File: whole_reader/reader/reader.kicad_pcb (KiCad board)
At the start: 2 copper layers, 50 x 58.5 mm, 66 parts, among them U1 LM386M-1, U2 STM32F103C8T6, U3 MCP16301Hx-xCH, U4 MAX3232, Y1 16MHz

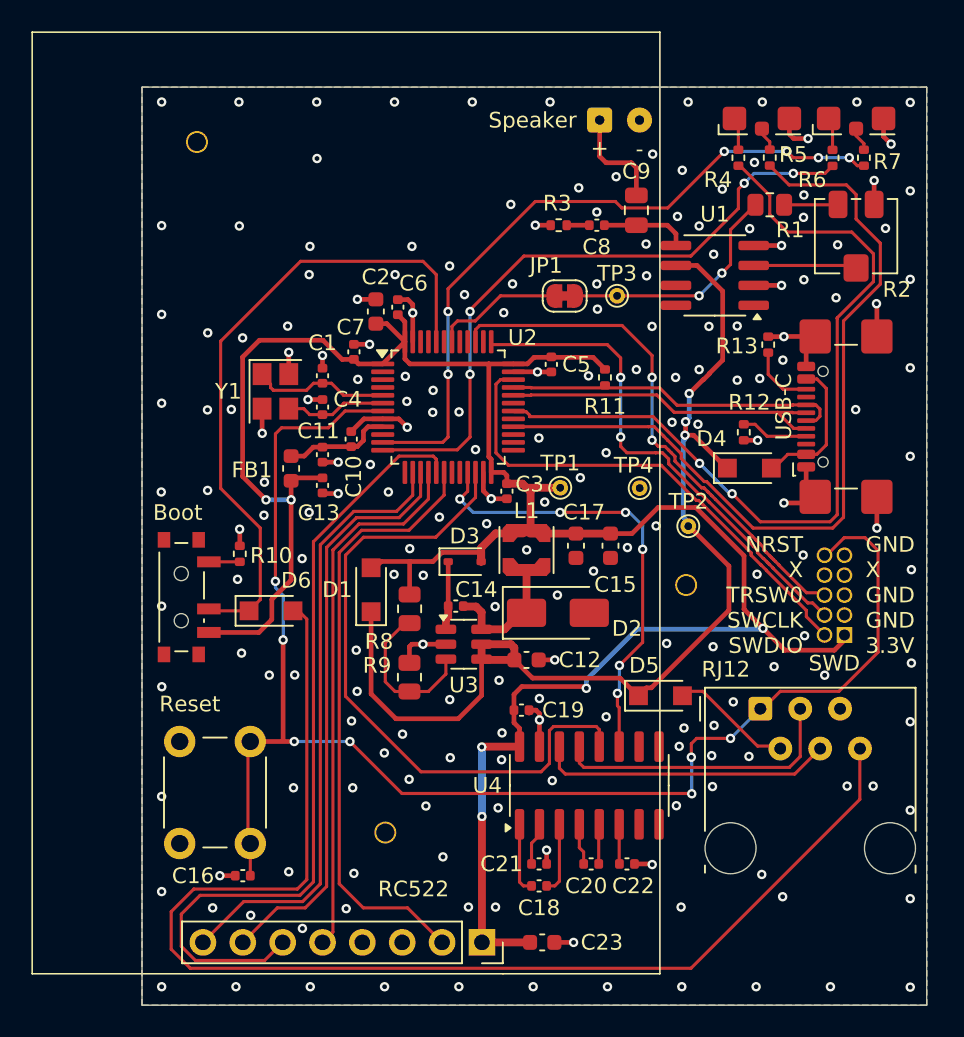
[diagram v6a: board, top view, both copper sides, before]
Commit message: Úprava rozloženia dosky a pridanie TP5 pre RFID_IRQ
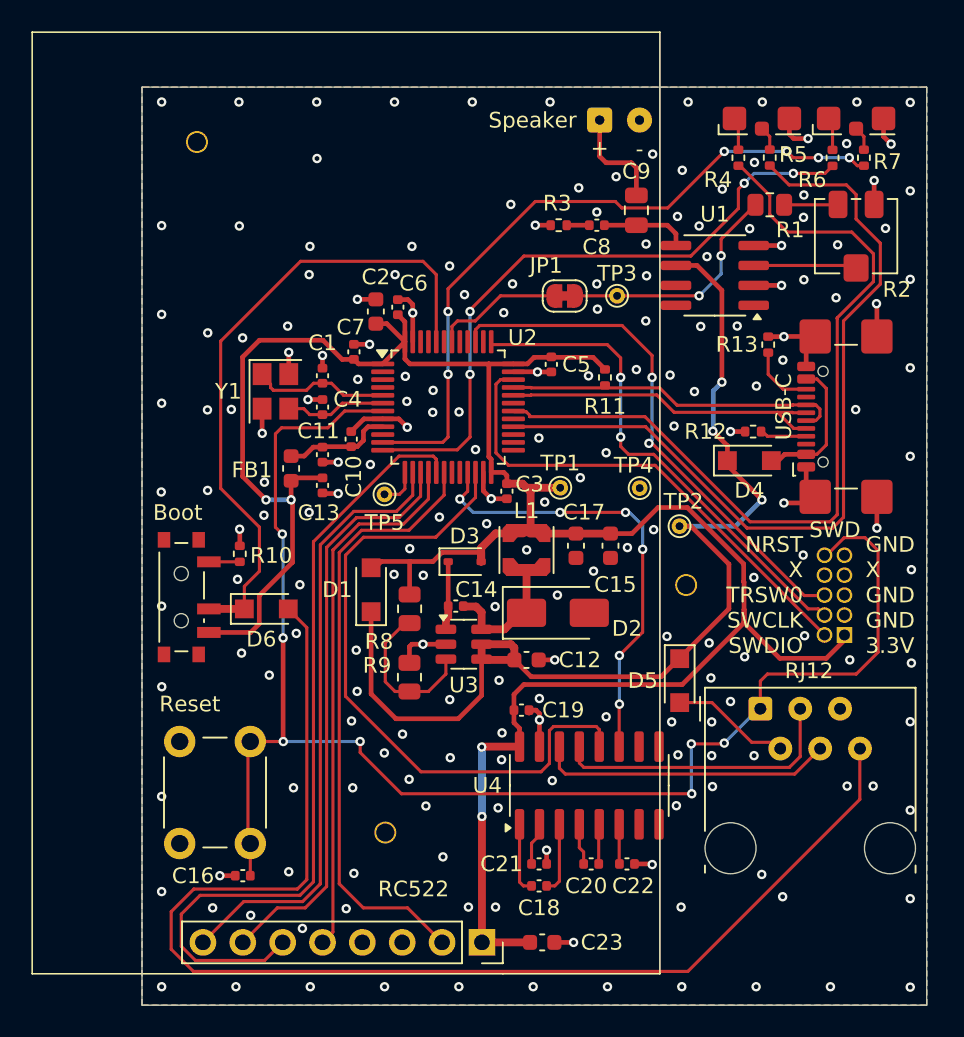
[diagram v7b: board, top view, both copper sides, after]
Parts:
- added TP5: RFID_IRQ, TestPoint:TestPoint_THTPad_D1.0mm_Drill0.5mm, F.Cu at (147.9, 53.5)
- moved D5 1.56 mm to (166.8, 65.3), turned to -90 degrees
- moved R12 0.60 mm to (171.4, 49.5), turned to 0 degrees
- moved TP2 0.56 mm to (166.8, 55.5)
- moved D4 0.48 mm to (171.2, 51.3)
- moved D6 0.32 mm to (140.4, 60.8)
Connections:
- U2 pad 13: unconnected-(U2-PA3-Pad13) -> RFID_IRQ
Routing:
- net RFID_IRQ: track 0.00 -> 2.49 mm
- net NRST: track 93.1 -> 94.6 mm
- net Net-(USB-C1-CC1): track 4.29 -> 3.04 mm
- net Net-(D4-A): track 9.25 -> 8.60 mm
- net V+: track 68.1 -> 68.7 mm
- net +3.3V: track 152.8 -> 152.5 mm, vias 6 -> 4
- net GND: track 56.2 -> 56.3 mm, vias 199 -> 198
- net LED_R1: vias 2 -> 0

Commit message: Pridane checkbox Tested
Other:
- board text added: "Tested"
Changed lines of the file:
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@@
 		(layer "F.SilkS")
 	)
+	(gr_rect
+		(start 177.05 80.575)
+		(end 179.95 83.425)
+		(stroke
+			(width 0.1)
+			(type solid)
+		)
+		(fill yes)
+		(layer "B.SilkS")
+	)
+	(gr_rect
+		(start 139.6 31.2)
+		(end 154.9 34.9)
+		(stroke
+			(width 0.3)
+			(type solid)
+		)
+		(fill no)
+		(layer "B.SilkS")
+	)
+	(gr_rect
+		(start 166.7 80.575)
+		(end 176.45 83.425)
+		(stroke
+			(width 0.1)
+			(type solid)
+		)
+		(fill no)
+		(layer "B.SilkS")
+	)
 	(gr_line
 		(start 182.5 84.5)
@@
 		)
 	)
+	(gr_text "Tested"
+		(at 176.45 82.1 0)
+		(layer "B.SilkS" knockout)
+		(effects
+			(font
+				(size 2 2)
+				(thickness 0.4)
+				(bold yes)
+			)
+			(justify left mirror)
+		)
+	)
 	(gr_text "UACS reader\nRev. 1.0 (2025/04)"
-		(at 155 34.2 0)
-		(layer "B.SilkS")
+		(at 154.95 34.3 0)
+		(layer "B.SilkS" knockout)
 		(effects
 			(font
 				(size 1 1)
-				(thickness 0.1)
+				(thickness 0.2)
+				(bold yes)
 			)
 			(justify left bottom mirror)
@@
 	)
 	(gr_text "JLCJLCJLCJLC"
-		(at 155 36.4 0)
+		(at 155.05 30.35 0)
 		(layer "B.SilkS")
 		(effects
@@
 	)
 	(gr_text "github.com/ostertag/UACS"
-		(at 148.6 30.2 0)
+		(at 155.05 35.9 0)
 		(layer "B.SilkS")
 		(effects
 			(font
 				(size 1 1)
-				(thickness 0.1)
+				(thickness 0.2)
+				(bold yes)
 			)
-			(justify bottom mirror)
+			(justify left top mirror)
 		)
 	)
@@
 	)
 	(via
-		(at 138.7 36.35)
+		(at 137.8 34.35)
 		(size 0.6)
 		(drill 0.3)
@@
 	)
 	(via
-		(at 149.7 37.65)
+		(at 148.6 37.8)
 		(size 0.6)
 		(drill 0.3)
@@
 	)
 	(via
-		(at 143.2 37.65)
+		(at 141.75 38.1)
 		(size 0.6)
 		(drill 0.3)
@@
 		)
 	)
+	(group ""
+		(members "177c4f97-1ffb-49b4-b03d-a0a92ce1235f" "626c5e70-a268-4187-9a4e-684bd983c42b"
+			"f957eb97-ddd9-4039-9f2b-52140d54414d"
+		)
+	)
